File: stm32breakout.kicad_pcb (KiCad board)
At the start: 2 copper layers, 60 x 80 mm, 42 parts, among them J1 USB_C_Receptacle_USB2.0_16P, J2 GPIO_LEFT, J3 GPIO_RIGHT, J4 SWD, SW1 NRST, SW2 BOOT0, U1 STM32F103C8Tx, U2 AP2112K-3.3, Y1 8MHz, Y2 32.768kHz

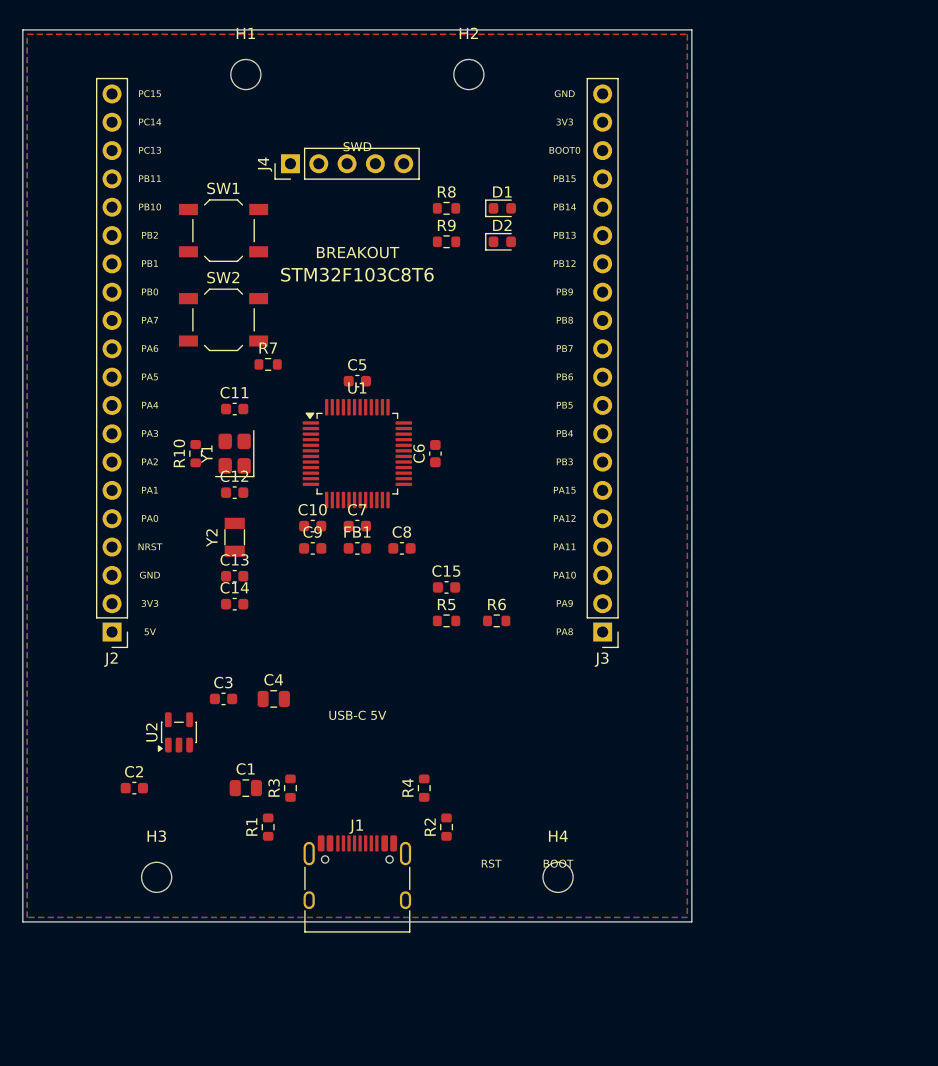
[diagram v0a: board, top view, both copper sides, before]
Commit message: Finish 2-layer routing and export JLCPCB fab files.
DRC is 0 geometry / 0 unconnected and ERC is 0. Analog filter
(FB1/C8/C9) is left of the MCU so last-mile +3V3/+3V3A and
NRST-to-J4 clear. Gerbers, LCSC BOM, and pick-and-place are in fab/.
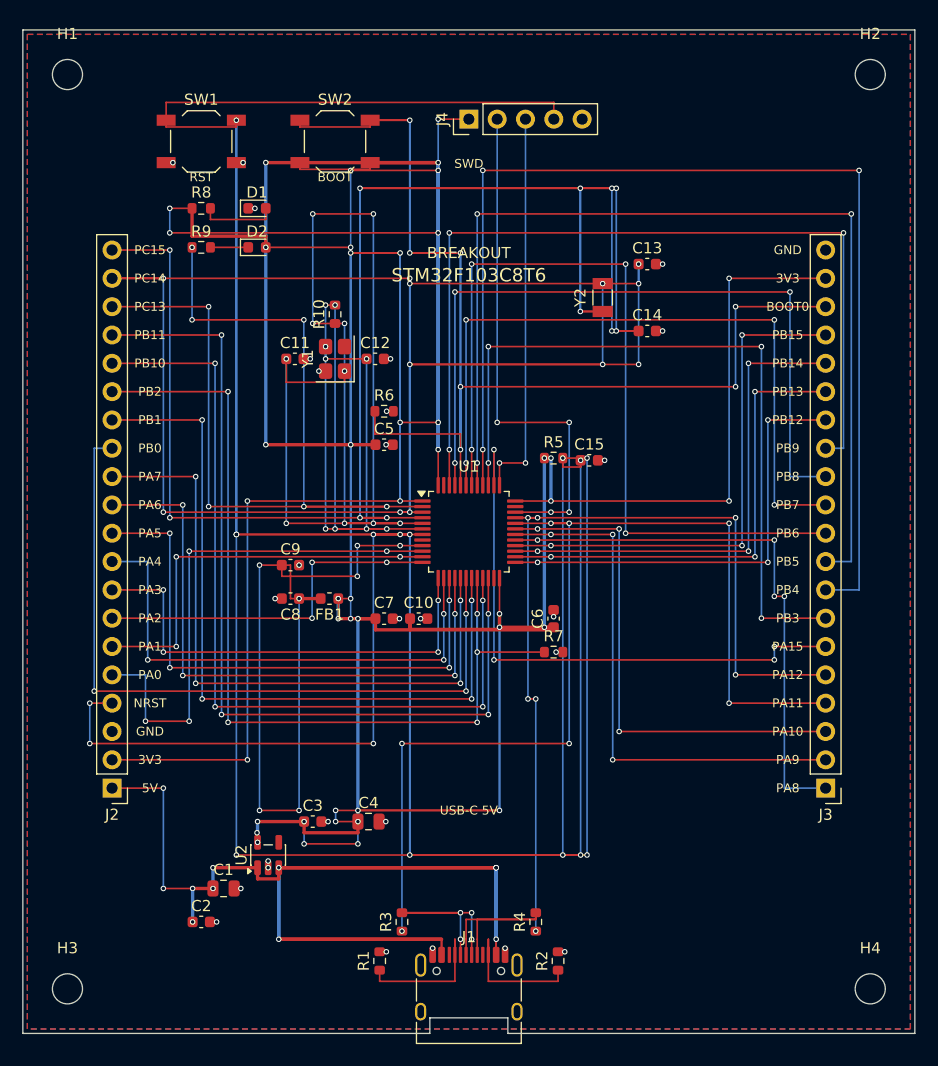
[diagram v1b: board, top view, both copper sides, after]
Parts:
- moved C13 46.4 mm to (56.0, 21.0)
- moved C14 44.4 mm to (56.0, 27.0)
- moved Y2 39.4 mm to (52.0, 24.0)
- moved R7 36.3 mm to (47.6, 55.8)
- moved H2 36.0 mm to (76.0, 4.00)
- moved H4 29.7 mm to (76.0, 86.0)
- moved J3 24.4 mm to (72.0, 68.0)
- moved D2 22.0 mm to (21.0, 19.5)
- moved R9 22.0 mm to (16.0, 19.5)
- moved D1 22.0 mm to (21.0, 16.0)
- moved R8 22.0 mm to (16.0, 16.0)
- moved R6 21.3 mm to (32.4, 34.2)
- moved SW2 18.9 mm to (28.0, 10.0)
- moved C6 18.2 mm to (47.6, 52.8)
- moved R10 17.7 mm to (28.0, 25.5)
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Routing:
- net +3V3: track 0.00 -> 718.7 mm, vias 0 -> 44
- net NRST: track 0.00 -> 500.7 mm, vias 0 -> 17
- net PC14: track 0.00 -> 223.3 mm, vias 0 -> 13
- net PC15: track 0.00 -> 217.4 mm, vias 0 -> 11
- net BOOT0: track 0.00 -> 142.7 mm, vias 0 -> 7
- net +5V: track 0.00 -> 132.1 mm, vias 0 -> 11
- net PD0: track 0.00 -> 106.5 mm, vias 0 -> 10
- net PB4: track 0.00 -> 102.6 mm, vias 0 -> 3
- net PA11: track 0.00 -> 97.2 mm, vias 0 -> 7
- net PB5: track 0.00 -> 91.4 mm, vias 0 -> 3
- net PC13: track 0.00 -> 86.5 mm, vias 0 -> 7
- net PB2: track 0.00 -> 84.8 mm, vias 0 -> 5
- net PA12: track 0.00 -> 80.6 mm, vias 0 -> 7
- net PB11: track 0.00 -> 80.0 mm, vias 0 -> 4
- net PB9: track 0.00 -> 78.9 mm, vias 0 -> 3
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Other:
- board size 60 x 80 mm -> 80 x 90 mm
